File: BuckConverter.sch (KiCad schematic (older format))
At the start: 0 parts

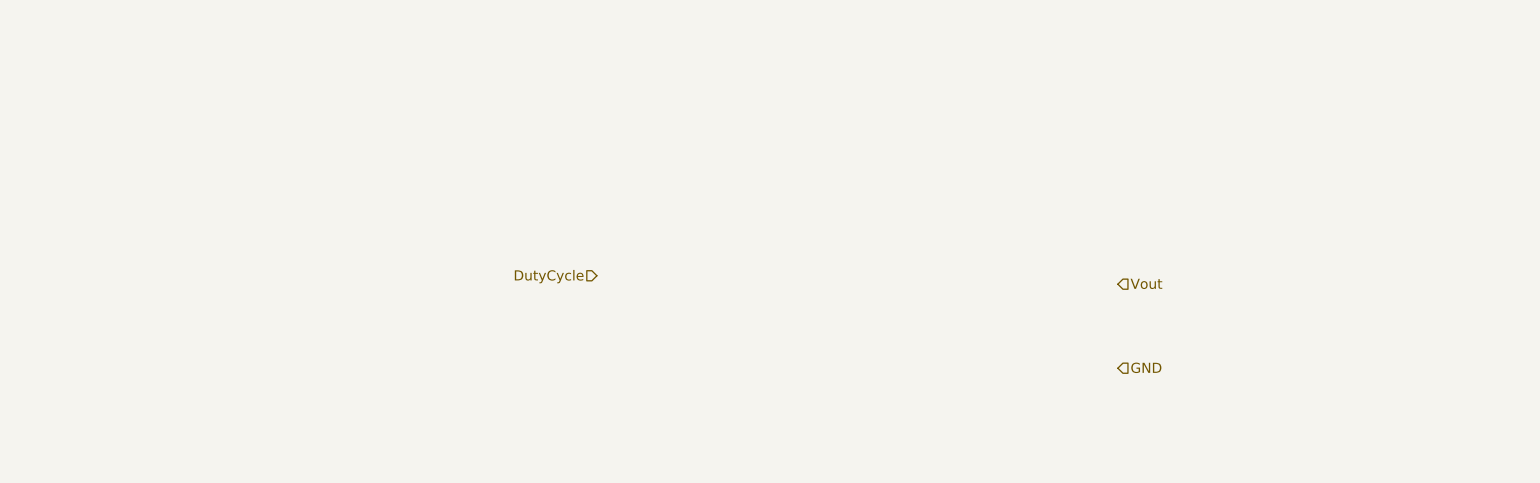
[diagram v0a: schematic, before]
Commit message: Added the basic Buck Schematic with the IRL2004
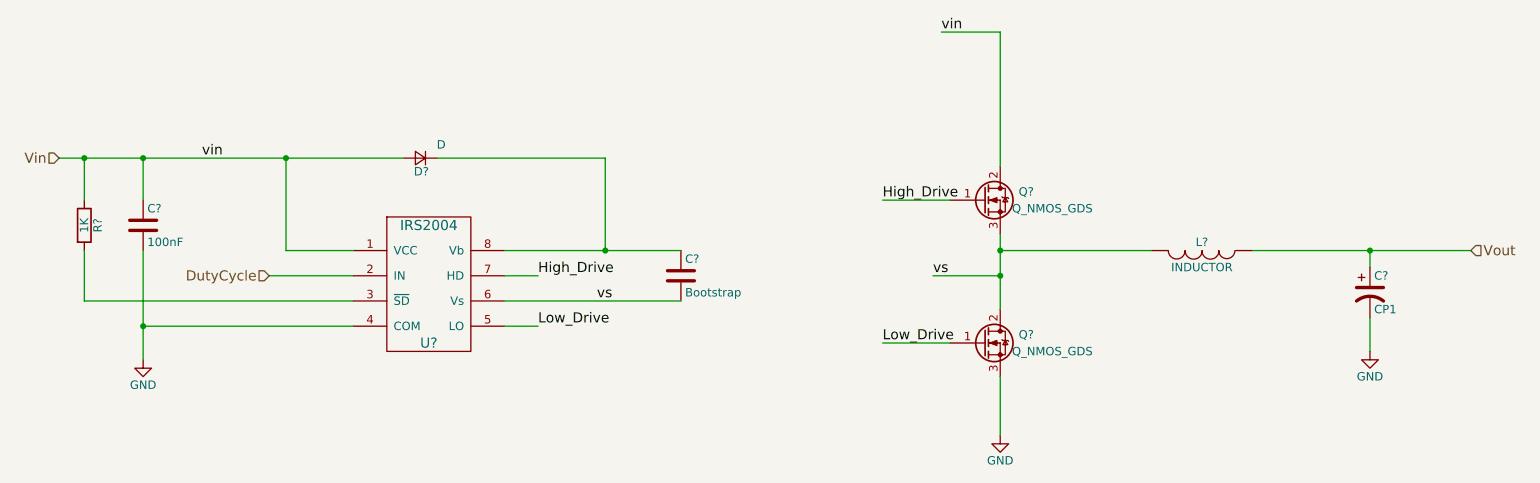
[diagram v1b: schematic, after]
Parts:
- added C?: 100nF, symbol C
- added C?: Bootstrap, symbol C
- added C?: CP1, symbol CP1
- added D?: D, symbol D_Small
- added L?: INDUCTOR, symbol INDUCTOR
- added Q? (x2): Q_NMOS_GDS, symbol Q_NMOS_GDS
- added R?: 1K, symbol R
- added U?: IRS2004, symbol IRS2004
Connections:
- net DutyCycle: now also U?.2 (IN)
- net GND: now also C?.2, C?.2, Q?.3 (S), U?.4 (COM)
- net Vout: now also C?.1, L?.1
- new net: R?.2, U?.3 (~SD)
- new net: C?.1, D?.1 (K), U?.8 (Vb)
- new net High_Drive: Q?.1 (G), U?.7 (HD)
- new net Low_Drive: Q?.1 (G), U?.5 (LO)
- new net Vin: C?.1, D?.2 (A), Q?.2 (D), R?.1, U?.1 (VCC)
- new net vs: C?.2, L?.2, Q?.2 (D), Q?.3 (S), U?.6 (Vs)
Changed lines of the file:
@@
 LIBS:valves
 LIBS:Buck Supply-cache
+LIBS:ir
 EELAYER 25 0
 EELAYER END
@@
 Comment4 ""
 $EndDescr
-Text HLabel 4300 3350 0    60   Input ~ 0
+Text HLabel 2350 3350 0    60   Input ~ 0
 DutyCycle
-Text HLabel 7400 3400 2    60   Input ~ 0
+Text HLabel 9500 3200 2    60   Input ~ 0
 Vout
-Text HLabel 7400 3900 2    60   Input ~ 0
-GND
+Text HLabel 1100 2650 0    60   Input ~ 0
+Vin
+$Comp
+L IRS2004 U?
+U 1 1 58B71DF7
+P 3300 3400
+F 0 "U?" H 3300 3050 60  0000 C CNN
+F 1 "IRS2004" H 3300 3750 60  0000 C CNN
+F 2 "" H 3350 3350 60  0000 C CNN
+F 3 "" H 3350 3350 60  0000 C CNN
+	1    3300 3400
+	1    0    0    -1
+$EndComp
+$Comp
+L R R?
+U 1 1 58B71E51
+P 1250 3050
+F 0 "R?" V 1330 3050 50  0000 C CNN
+F 1 "1K" V 1250 3050 50  0000 C CNN
+F 2 "" V 1180 3050 50  0000 C CNN
+F 3 "" H 1250 3050 50  0000 C CNN
+	1    1250 3050
+	1    0    0    -1
+$EndComp
+$Comp
+L GND #PWR?
+U 1 1 58B71E95
+P 1600 3850
+F 0 "#PWR?" H 1600 3600 50  0001 C CNN
+F 1 "GND" H 1600 3700 50  0000 C CNN
+F 2 "" H 1600 3850 50  0000 C CNN
+F 3 "" H 1600 3850 50  0000 C CNN
+	1    1600 3850
+	1    0    0    -1
+$EndComp
+$Comp
+L C C?
+U 1 1 58B71F54
+P 1600 3050
+F 0 "C?" H 1625 3150 50  0000 L CNN
+F 1 "100nF" H 1625 2950 50  0000 L CNN
+F 2 "" H 1638 2900 50  0000 C CNN
+F 3 "" H 1600 3050 50  0000 C CNN
+	1    1600 3050
+	1    0    0    -1
+$EndComp
+$Comp
+L D_Small D?
+U 1 1 58B720C2
+P 3250 2650
+F 0 "D?" H 3200 2730 50  0000 L CNN
+F 1 "D" H 3100 2570 50  0000 L CNN
+F 2 "" V 3250 2650 50  0000 C CNN
+F 3 "" V 3250 2650 50  0000 C CNN
+	1    3250 2650
+	-1   0    0    1
+$EndComp
+$Comp
+L C C?
+U 1 1 58B724B3
+P 4800 3350
+F 0 "C?" H 4825 3450 50  0000 L CNN
+F 1 "Bootstrap" H 4825 3250 50  0000 L CNN
+F 2 "" H 4838 3200 50  0000 C CNN
+F 3 "" H 4800 3350 50  0000 C CNN
+	1    4800 3350
+	1    0    0    -1
+$EndComp
+Text Label 3950 3350 0    60   ~ 0
+High_Drive
+Text Label 3950 3650 0    60   ~ 0
+Low_Drive
+$Comp
+L Q_NMOS_GDS Q?
+U 1 1 58B72E81
+P 6600 2900
+F 0 "Q?" H 6900 2950 50  0000 R CNN
+F 1 "Q_NMOS_GDS" H 7250 2850 50  0000 R CNN
+F 2 "" H 6800 3000 50  0000 C CNN
+F 3 "" H 6600 2900 50  0000 C CNN
+	1    6600 2900
+	1    0    0    -1
+$EndComp
+$Comp
+L Q_NMOS_GDS Q?
+U 1 1 58B72EC6
+P 6600 3750
+F 0 "Q?" H 6900 3800 50  0000 R CNN
+F 1 "Q_NMOS_GDS" H 7250 3700 50  0000 R CNN
+F 2 "" H 6800 3850 50  0000 C CNN
+F 3 "" H 6600 3750 50  0000 C CNN
+	1    6600 3750
+	1    0    0    -1
+$EndComp
+Text Label 1950 2650 0    60   ~ 0
+vin
+Wire Wire Line
+	2350 3350 2850 3350
+Wire Wire Line
+	1100 2650 3150 2650
+Wire Wire Line
+	1250 2650 1250 2900
+Wire Wire Line
+	1250 3200 1250 3500
+Wire Wire Line
+	1250 3500 2850 3500
+Wire Wire Line
+	1600 2650 1600 2900
+Connection ~ 1250 2650
+Wire Wire Line
+	2850 3650 1600 3650
+Wire Wire Line
+	1600 3200 1600 3850
+Connection ~ 1600 3650
+Connection ~ 1600 2650
+Wire Wire Line
+	2850 3200 2450 3200
+Wire Wire Line
+	2450 3200 2450 2650
+Connection ~ 2450 2650
+Wire Wire Line
+	3750 3500 4800 3500
+Wire Wire Line
+	3750 3200 4800 3200
+Wire Wire Line
+	3350 2650 4350 2650
+Wire Wire Line
+	4350 2650 4350 3200
+Connection ~ 4350 3200
+Wire Wire Line
+	3750 3350 3950 3350
+Wire Wire Line
+	3750 3650 3950 3650
+Wire Wire Line
+	6700 3100 6700 3550
+Wire Wire Line
+	6700 3350 6300 3350
+Connection ~ 6700 3350
+Text Label 4300 3500 0    60   ~ 0
+vs
+Text Label 6300 3350 0    60   ~ 0
+vs
+Wire Wire Line
+	6400 2900 6000 2900
+Wire Wire Line
+	6400 3750 6000 3750
+Text Label 6000 2900 0    60   ~ 0
+High_Drive
+Text Label 6000 3750 0    60   ~ 0
+Low_Drive
+$Comp
+L GND #PWR?
+U 1 1 58B7404F
+P 6700 4300
+F 0 "#PWR?" H 6700 4050 50  0001 C CNN
+F 1 "GND" H 6700 4150 50  0000 C CNN
+F 2 "" H 6700 4300 50  0000 C CNN
+F 3 "" H 6700 4300 50  0000 C CNN
+	1    6700 4300
+	1    0    0    -1
+$EndComp
+Wire Wire Line
+	6700 3950 6700 4300
+Wire Wire Line
+	6700 2700 6700 1900
+Wire Wire Line
+	6700 1900 6350 1900
+Text Label 6350 1900 0    60   ~ 0
+vin
+$Comp
+L INDUCTOR L?
+U 1 1 58B74E09
+P 7900 3200
+F 0 "L?" V 7850 3200 50  0000 C CNN
+F 1 "INDUCTOR" V 8000 3200 50  0000 C CNN
+F 2 "" H 7900 3200 50  0000 C CNN
+F 3 "" H 7900 3200 50  0000 C CNN
+	1    7900 3200
+	0    1    1    0
+$EndComp
+Wire Wire Line
+	9500 3200 8200 3200
+Wire Wire Line
+	7600 3200 6700 3200
+Connection ~ 6700 3200
+$Comp
+L CP1 C?
+U 1 1 58B74ED9
+P 8900 3450
+F 0 "C?" H 8925 3550 50  0000 L CNN
+F 1 "CP1" H 8925 3350 50  0000 L CNN
+F 2 "" H 8900 3450 50  0000 C CNN
+F 3 "" H 8900 3450 50  0000 C CNN
+	1    8900 3450
+	1    0    0    -1
+$EndComp
+Wire Wire Line
+	8900 3300 8900 3200
+Connection ~ 8900 3200
+$Comp
+L GND #PWR?
+U 1 1 58B75099
+P 8900 3800
+F 0 "#PWR?" H 8900 3550 50  0001 C CNN
+F 1 "GND" H 8900 3650 50  0000 C CNN
+F 2 "" H 8900 3800 50  0000 C CNN
+F 3 "" H 8900 3800 50  0000 C CNN
+	1    8900 3800
+	1    0    0    -1
+$EndComp
+Wire Wire Line
+	8900 3600 8900 3800
 $EndSCHEMATC

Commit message: Finished the full circuit.
All thats left is to set the design parameters.
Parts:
- added D?: IN4007, symbol D
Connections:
- net GND: now also D?.2 (A)
- net vs: now also D?.1 (K)
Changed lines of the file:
@@
 $Descr A4 11693 8268
 encoding utf-8
-Sheet 5 5
+Sheet 5 4
 Title ""
 Date ""
@@
 Wire Wire Line
 	8900 3600 8900 3800
+$Comp
+L D D?
+U 1 1 58B84A7B
+P 7450 3450
+F 0 "D?" H 7450 3550 50  0000 C CNN
+F 1 "IN4007" H 7450 3350 50  0000 C CNN
+F 2 "" H 7450 3450 50  0000 C CNN
+F 3 "" H 7450 3450 50  0000 C CNN
+	1    7450 3450
+	0    1    1    0
+$EndComp
+Wire Wire Line
+	7450 3300 7450 3200
+Connection ~ 7450 3200
+$Comp
+L GND #PWR?
+U 1 1 58B84B0B
+P 7450 3700
+F 0 "#PWR?" H 7450 3450 50  0001 C CNN
+F 1 "GND" H 7450 3550 50  0000 C CNN
+F 2 "" H 7450 3700 50  0000 C CNN
+F 3 "" H 7450 3700 50  0000 C CNN
+	1    7450 3700
+	1    0    0    -1
+$EndComp
+Wire Wire Line
+	7450 3600 7450 3700
 $EndSCHEMATC

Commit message: Did a whole bunch of layout
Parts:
- C3, C4: renamed from C?; footprint (none) -> Capacitors_THT:C_Disc_D3_P2.5
- C5: renamed from C?; footprint (none) -> Capacitors_THT:C_Radial_D16_L30_P7.5
- D1: renamed from D?; footprint (none) -> Diodes_THT:Diode_DO-35_SOD27_Horizontal_RM10
- D2: renamed from D?; footprint (none) -> Diodes_THT:Diode_DO-41_SOD81_Horizontal_RM10
- L1: renamed from L?; footprint (none) -> Inductors_NEOSID:Neosid_Inductor_Sd75
- Q3, Q4: renamed from Q?; footprint (none) -> TO_SOT_Packages_THT:TO-220_Neutral123_Horizontal
- R12: renamed from R?; footprint (none) -> Resistors_THT:Resistor_Horizontal_RM7mm
- U5: renamed from U?; footprint (none) -> Housings_DIP:DIP-8_W7.62mm_LongPads
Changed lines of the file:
@@
 $Descr A4 11693 8268
 encoding utf-8
-Sheet 5 4
+Sheet 4 4
 Title ""
 Date ""
@@
 Vin
 $Comp
-L IRS2004 U?
+L IRS2004 U5
 U 1 1 58B71DF7
 P 3300 3400
-F 0 "U?" H 3300 3050 60  0000 C CNN
+F 0 "U5" H 3300 3050 60  0000 C CNN
 F 1 "IRS2004" H 3300 3750 60  0000 C CNN
-F 2 "" H 3350 3350 60  0000 C CNN
+F 2 "Housings_DIP:DIP-8_W7.62mm_LongPads" H 3350 3350 60  0001 C CNN
 F 3 "" H 3350 3350 60  0000 C CNN
 	1    3300 3400
@@
 $EndComp
 $Comp
-L R R?
+L R R12
 U 1 1 58B71E51
 P 1250 3050
-F 0 "R?" V 1330 3050 50  0000 C CNN
+F 0 "R12" V 1330 3050 50  0000 C CNN
 F 1 "1K" V 1250 3050 50  0000 C CNN
-F 2 "" V 1180 3050 50  0000 C CNN
+F 2 "Resistors_THT:Resistor_Horizontal_RM7mm" V 1180 3050 50  0001 C CNN
 F 3 "" H 1250 3050 50  0000 C CNN
 	1    1250 3050
@@
 $EndComp
 $Comp
-L GND #PWR?
+L GND #PWR022
 U 1 1 58B71E95
 P 1600 3850
-F 0 "#PWR?" H 1600 3600 50  0001 C CNN
+F 0 "#PWR022" H 1600 3600 50  0001 C CNN
 F 1 "GND" H 1600 3700 50  0000 C CNN
 F 2 "" H 1600 3850 50  0000 C CNN
@@
 $EndComp
 $Comp
-L C C?
+L C C3
 U 1 1 58B71F54
 P 1600 3050
-F 0 "C?" H 1625 3150 50  0000 L CNN
+F 0 "C3" H 1625 3150 50  0000 L CNN
 F 1 "100nF" H 1625 2950 50  0000 L CNN
-F 2 "" H 1638 2900 50  0000 C CNN
+F 2 "Capacitors_THT:C_Disc_D3_P2.5" H 1638 2900 50  0001 C CNN
 F 3 "" H 1600 3050 50  0000 C CNN
 	1    1600 3050
@@
 $EndComp
 $Comp
-L D_Small D?
+L D_Small D1
 U 1 1 58B720C2
 P 3250 2650
-F 0 "D?" H 3200 2730 50  0000 L CNN
+F 0 "D1" H 3200 2730 50  0000 L CNN
 F 1 "D" H 3100 2570 50  0000 L CNN
-F 2 "" V 3250 2650 50  0000 C CNN
+F 2 "Diodes_THT:Diode_DO-35_SOD27_Horizontal_RM10" V 3250 2650 50  0001 C CNN
 F 3 "" V 3250 2650 50  0000 C CNN
 	1    3250 2650
@@
 $EndComp
 $Comp
-L C C?
+L C C4
 U 1 1 58B724B3
 P 4800 3350
-F 0 "C?" H 4825 3450 50  0000 L CNN
+F 0 "C4" H 4825 3450 50  0000 L CNN
 F 1 "Bootstrap" H 4825 3250 50  0000 L CNN
-F 2 "" H 4838 3200 50  0000 C CNN
+F 2 "Capacitors_THT:C_Disc_D3_P2.5" H 4838 3200 50  0001 C CNN
 F 3 "" H 4800 3350 50  0000 C CNN
 	1    4800 3350
@@
 Low_Drive
 $Comp
-L Q_NMOS_GDS Q?
+L Q_NMOS_GDS Q3
 U 1 1 58B72E81
 P 6600 2900
-F 0 "Q?" H 6900 2950 50  0000 R CNN
+F 0 "Q3" H 6900 2950 50  0000 R CNN
 F 1 "Q_NMOS_GDS" H 7250 2850 50  0000 R CNN
-F 2 "" H 6800 3000 50  0000 C CNN
+F 2 "TO_SOT_Packages_THT:TO-220_Neutral123_Horizontal" H 6800 3000 50  0001 C CNN
 F 3 "" H 6600 2900 50  0000 C CNN
 	1    6600 2900
@@
 $EndComp
 $Comp
-L Q_NMOS_GDS Q?
+L Q_NMOS_GDS Q4
 U 1 1 58B72EC6
 P 6600 3750
-F 0 "Q?" H 6900 3800 50  0000 R CNN
+F 0 "Q4" H 6900 3800 50  0000 R CNN
 F 1 "Q_NMOS_GDS" H 7250 3700 50  0000 R CNN
-F 2 "" H 6800 3850 50  0000 C CNN
+F 2 "TO_SOT_Packages_THT:TO-220_Neutral123_Horizontal" H 6800 3850 50  0001 C CNN
 F 3 "" H 6600 3750 50  0000 C CNN
 	1    6600 3750
@@
 Low_Drive
 $Comp
-L GND #PWR?
+L GND #PWR023
 U 1 1 58B7404F
 P 6700 4300
-F 0 "#PWR?" H 6700 4050 50  0001 C CNN
+F 0 "#PWR023" H 6700 4050 50  0001 C CNN
 F 1 "GND" H 6700 4150 50  0000 C CNN
 F 2 "" H 6700 4300 50  0000 C CNN
@@
 vin
 $Comp
-L INDUCTOR L?
+L INDUCTOR L1
 U 1 1 58B74E09
 P 7900 3200
-F 0 "L?" V 7850 3200 50  0000 C CNN
+F 0 "L1" V 7850 3200 50  0000 C CNN
 F 1 "INDUCTOR" V 8000 3200 50  0000 C CNN
-F 2 "" H 7900 3200 50  0000 C CNN
+F 2 "Inductors_NEOSID:Neosid_Inductor_Sd75" H 7900 3200 50  0001 C CNN
 F 3 "" H 7900 3200 50  0000 C CNN
 	1    7900 3200
@@
 Connection ~ 6700 3200
 $Comp
-L CP1 C?
+L CP1 C5
 U 1 1 58B74ED9
 P 8900 3450
-F 0 "C?" H 8925 3550 50  0000 L CNN
+F 0 "C5" H 8925 3550 50  0000 L CNN
 F 1 "CP1" H 8925 3350 50  0000 L CNN
-F 2 "" H 8900 3450 50  0000 C CNN
+F 2 "Capacitors_THT:C_Radial_D16_L30_P7.5" H 8900 3450 50  0001 C CNN
 F 3 "" H 8900 3450 50  0000 C CNN
 	1    8900 3450
@@
 Connection ~ 8900 3200
 $Comp
-L GND #PWR?
+L GND #PWR024
 U 1 1 58B75099
 P 8900 3800
-F 0 "#PWR?" H 8900 3550 50  0001 C CNN
+F 0 "#PWR024" H 8900 3550 50  0001 C CNN
 F 1 "GND" H 8900 3650 50  0000 C CNN
 F 2 "" H 8900 3800 50  0000 C CNN
@@
 	8900 3600 8900 3800
 $Comp
-L D D?
+L D D2
 U 1 1 58B84A7B
 P 7450 3450
-F 0 "D?" H 7450 3550 50  0000 C CNN
+F 0 "D2" H 7450 3550 50  0000 C CNN
 F 1 "IN4007" H 7450 3350 50  0000 C CNN
-F 2 "" H 7450 3450 50  0000 C CNN
+F 2 "Diodes_THT:Diode_DO-41_SOD81_Horizontal_RM10" H 7450 3450 50  0001 C CNN
 F 3 "" H 7450 3450 50  0000 C CNN
 	1    7450 3450
@@
 Connection ~ 7450 3200
 $Comp
-L GND #PWR?
+L GND #PWR025
 U 1 1 58B84B0B
 P 7450 3700
-F 0 "#PWR?" H 7450 3450 50  0001 C CNN
+F 0 "#PWR025" H 7450 3450 50  0001 C CNN
 F 1 "GND" H 7450 3550 50  0000 C CNN
 F 2 "" H 7450 3700 50  0000 C CNN
